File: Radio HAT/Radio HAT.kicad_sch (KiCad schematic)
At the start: 5 parts, among them J1 Raspberry_Pi_2_3, J2 Coax SMA, U1 RFM98PW

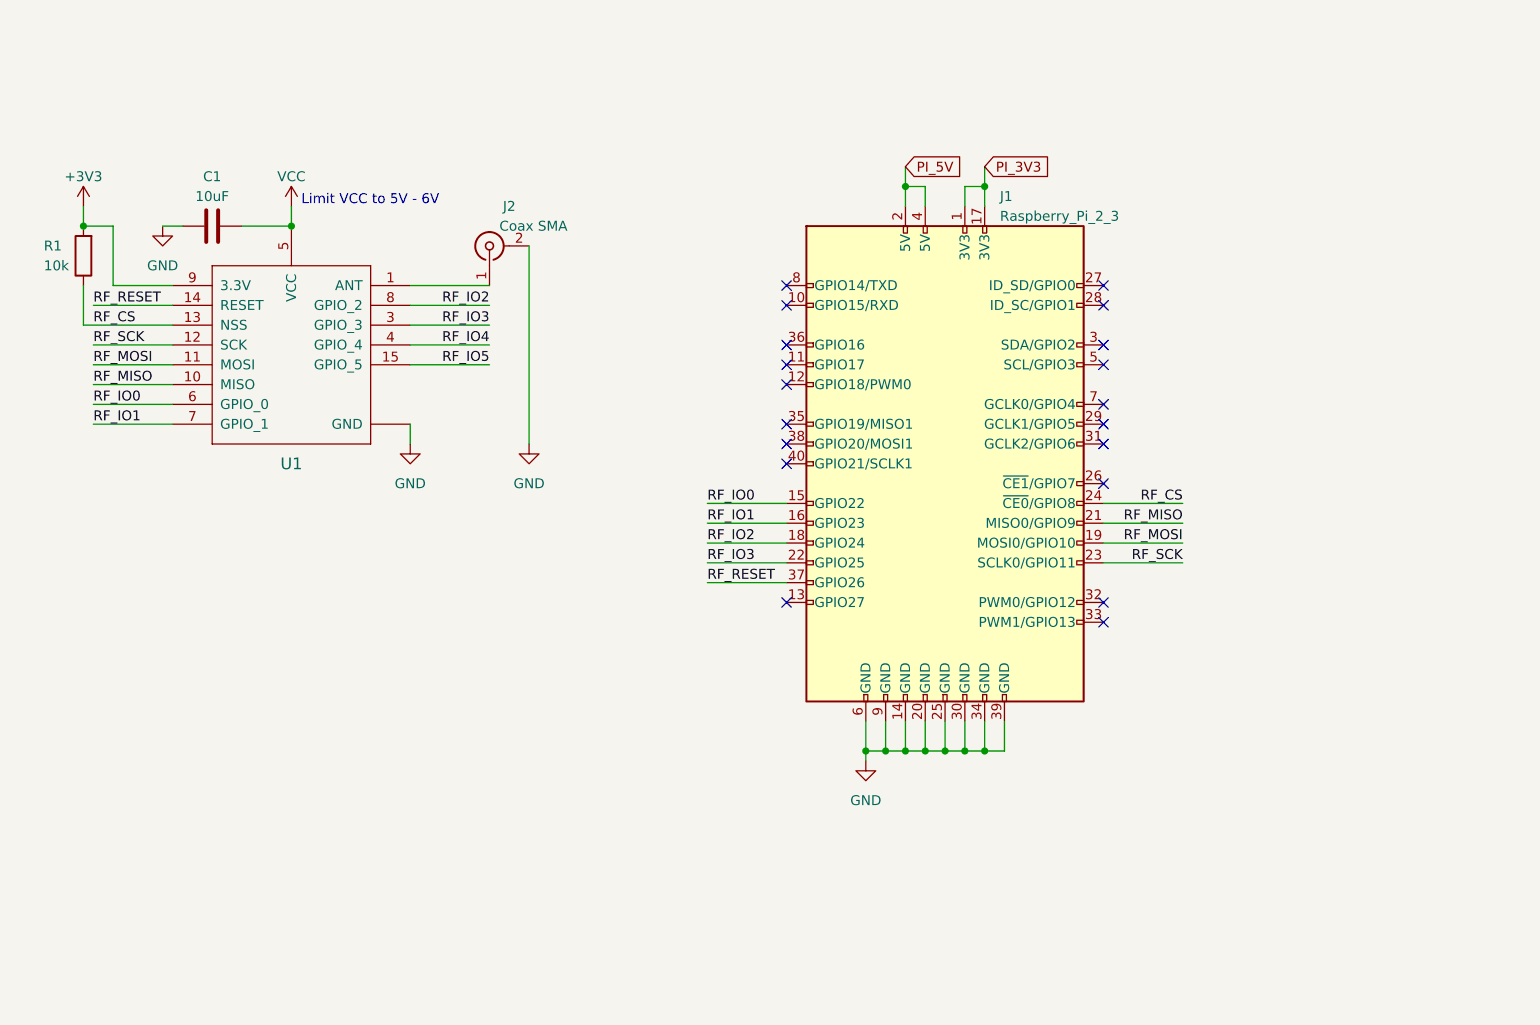
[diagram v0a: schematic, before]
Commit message: Finished schematic, started board layout
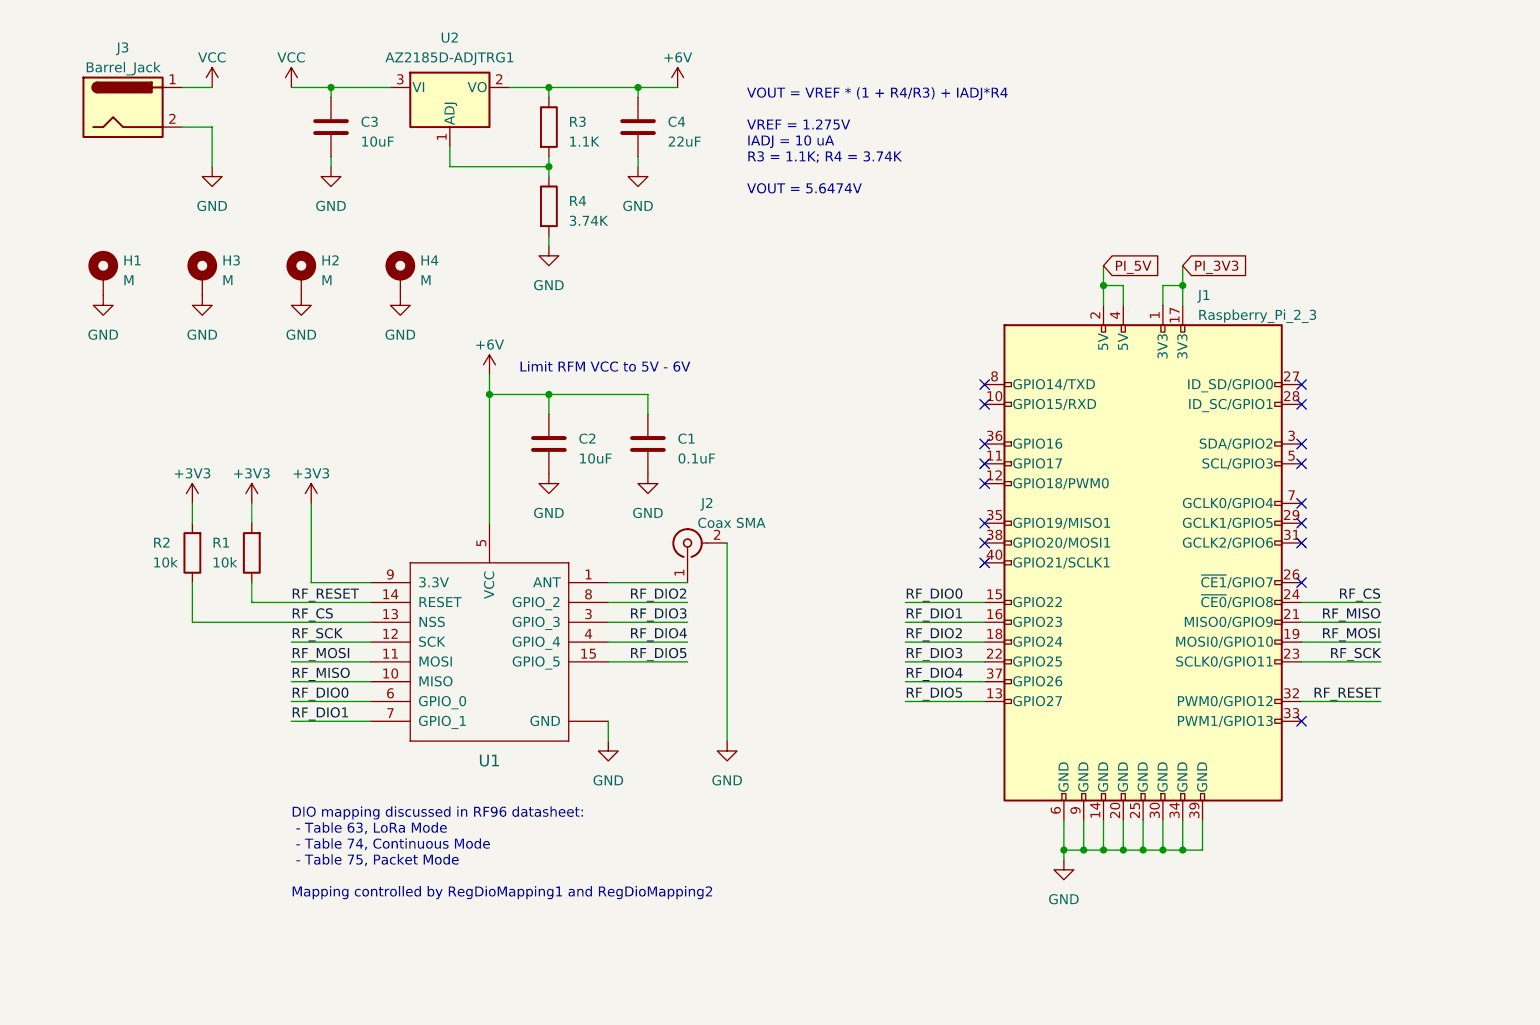
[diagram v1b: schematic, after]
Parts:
- added C2, C3: 10uF, Capacitor_SMD:C_0805_2012Metric_Pad1.18x1.45mm_HandSolder, symbol Device:C
- added C4: 22uF, Capacitor_SMD:C_0805_2012Metric_Pad1.18x1.45mm_HandSolder, symbol Device:C
- added H1, H2, H3, H4: M, MountingHole:MountingHole_2.7mm_M2.5_Pad_Via, symbol Mechanical:MountingHole_Pad
- added J3: Barrel_Jack, Connector_BarrelJack:BarrelJack_Horizontal, symbol Connector:Barrel_Jack
- added R2: 10k, Resistor_SMD:R_0805_2012Metric_Pad1.20x1.40mm_HandSolder, symbol Device:R
- added R3: 1.1K, Resistor_SMD:R_0805_2012Metric_Pad1.20x1.40mm_HandSolder, symbol Device:R
- added R4: 3.74K, Resistor_SMD:R_0805_2012Metric_Pad1.20x1.40mm_HandSolder, symbol Device:R
- added U2: AZ2185D-ADJTRG1, Package_TO_SOT_SMD:TO-252-2, symbol Regulator_Linear:NCP1117-ADJ_TO252
- C1: value 10uF -> 0.1uF; footprint (none) -> Capacitor_SMD:C_0805_2012Metric_Pad1.18x1.45mm_HandSolder
- J1: footprint (none) -> Connector_PinSocket_2.54mm:PinSocket_2x20_P2.54mm_Vertical
- J2: footprint (none) -> Connector_Coaxial:SMA_Amphenol_901-144_Vertical
- R1: footprint (none) -> Resistor_SMD:R_0805_2012Metric_Pad1.20x1.40mm_HandSolder
- U1: footprint custom-footprints:RFM95PW -> Mainboard:RFM95PW
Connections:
- net RF_IO5 is gone; now on net RF_DIO5: U1.15 (GPIO_5)
- net +3V3: now also R2.2
- net GND: now also C1.2, C2.2, C3.2, C4.2, H1.1, H2.1, H3.1, H4.1, J3.2, R4.2; no longer C1.1
- net RF_CS: now also R2.1; no longer R1.1
- net RF_RESET: now also J1.32 (PWM0/GPIO12), R1.1; no longer J1.37 (GPIO26)
- net VCC: now also C3.1, J3.1, U2.3 (VI); no longer C1.2, U1.5 (VCC)
- net RF_DIO5: now reaches J1.13 (GPIO27)
- net RF_IO0 renamed RF_DIO0
- net RF_IO1 renamed RF_DIO1
- net RF_IO2 renamed RF_DIO2
- net RF_IO3 renamed RF_DIO3
- net RF_IO4 renamed RF_DIO4
- net RF_DIO4: now also J1.37 (GPIO26)
- new net: R3.2, R4.1, U2.1 (ADJ)
- new net +6V: C1.1, C2.1, C4.1, R3.1, U1.5 (VCC), U2.2 (VO)
- no-connect marks 19 -> 17
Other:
- note added: "DIO mapping discussed in RF96 datasheet: - Table 63, LoRa Mode - Table 74, Continuous Mode - Table 75, Packet Mode Mapping controlled by RegDioMapping1 and RegDioMapping2"
- note added: "Limit RFM VCC to 5V - 6V"
- note added: "VOUT = VREF * (1 + R4/R3) + IADJ*R4 VREF = 1.275V IADJ = 10 uA R3 = 1.1K; R4 = 3.74K VOUT = 5.6474V"
- note removed: "Limit VCC to 5V - 6V"
- moved on the sheet: J1, J2, R1, U1

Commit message: Finished board design
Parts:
- removed H3, H4: M, MountingHole:MountingHole_2.7mm_M2.5_Pad_Via, symbol Mechanical:MountingHole_Pad
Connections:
- net RF_DIO0: now also J1.35 (GPIO19/MISO1); no longer J1.15 (GPIO22)
- net RF_DIO1: now also J1.38 (GPIO20/MOSI1); no longer J1.16 (GPIO23)
- net RF_DIO2: now also J1.40 (GPIO21/SCLK1); no longer J1.18 (GPIO24)
- net RF_DIO3: now also J1.33 (PWM1/GPIO13); no longer J1.22 (GPIO25)
- net RF_DIO5: now also J1.36 (GPIO16); no longer J1.13 (GPIO27)
- net RF_ANT: now reaches J2.1 (In), U1.1 (ANT)
- net REG_ADJ: now reaches R3.2, R4.1, U2.1 (ADJ)
- net PI_3V3: no longer names the net of J1.1 (3V3)
- net PI_3V3: no longer J1.17 (3V3)
- net PI_5V: no longer names the net of J1.2 (5V)
- net PI_5V: no longer J1.4 (5V)
- no-connect marks 17 -> 21
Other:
- moved on the sheet: H1, J2

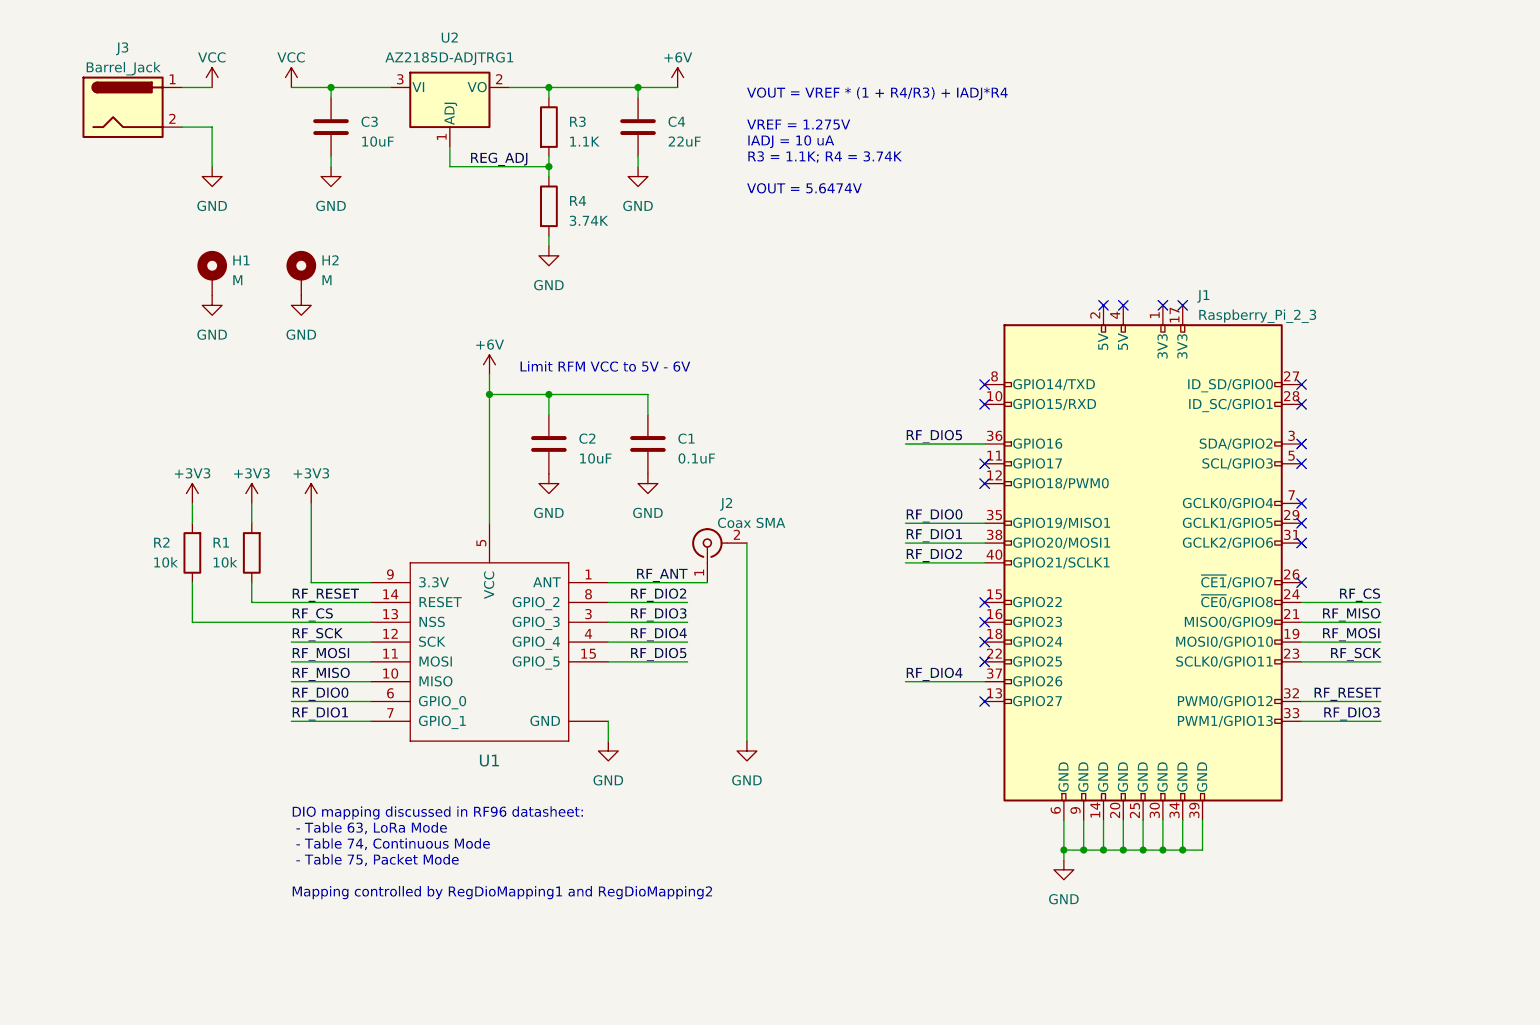
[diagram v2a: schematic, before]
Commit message: Implemented changes from PR review
Changes implemented:
 - added schematic documentation and page settings
 - fixed PCB silkscreen
 - added board rev. and information on back silkscreen
 - added 3D models, generated 3D model for board
 - generated HTML BOM
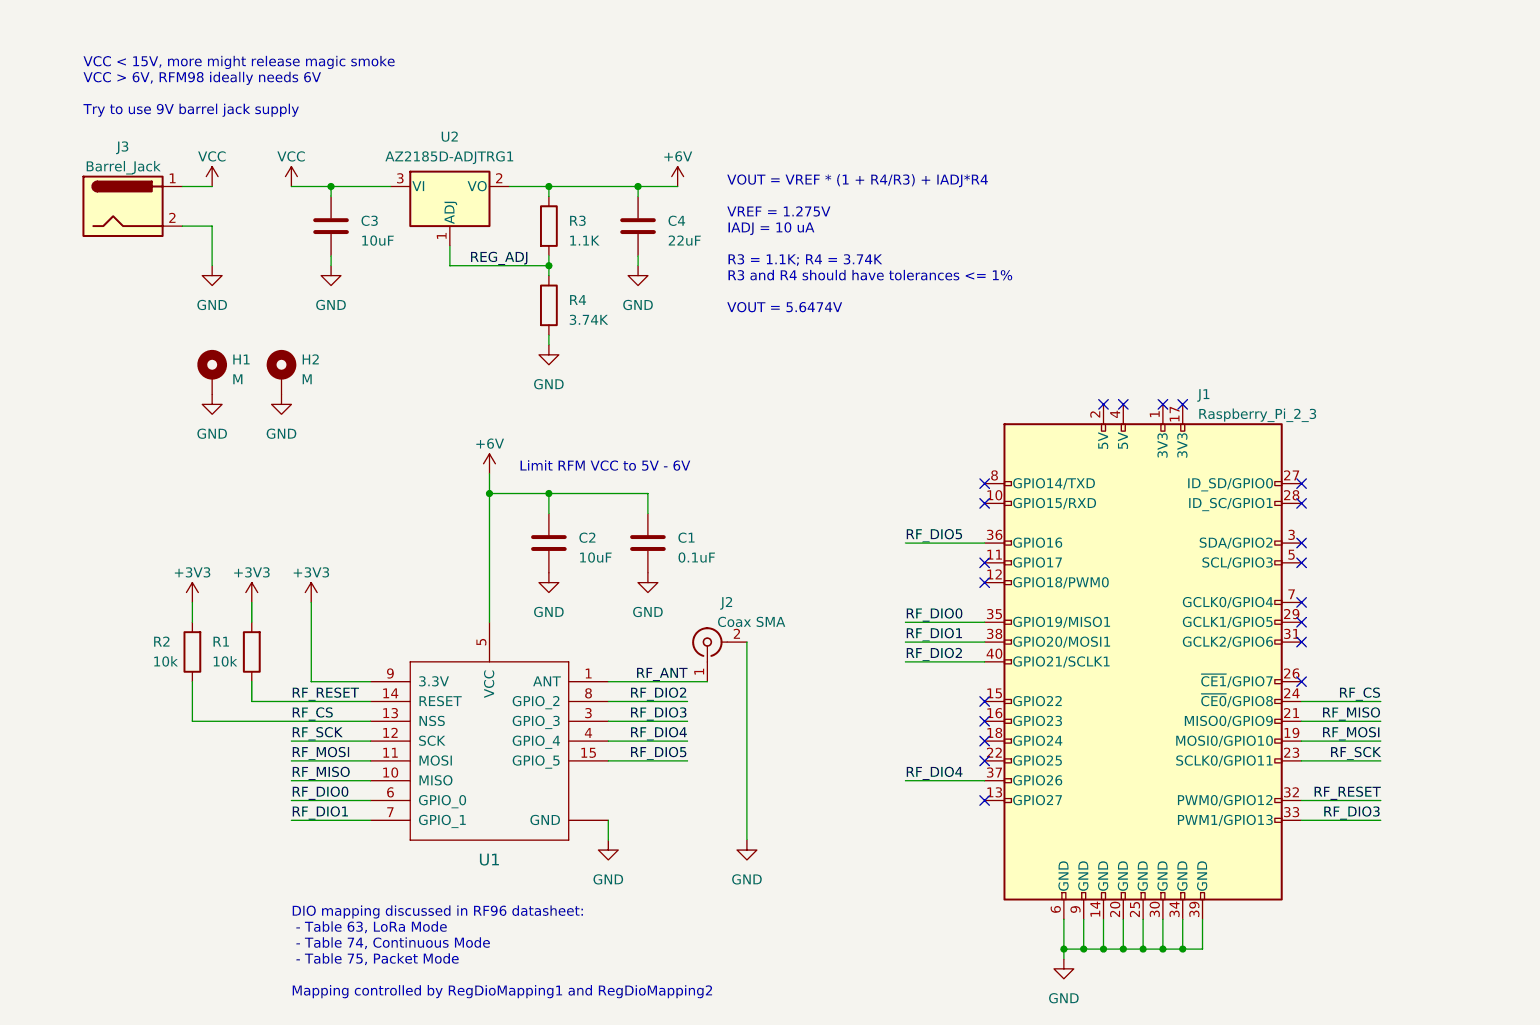
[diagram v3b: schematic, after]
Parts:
- removed U1: RFM98PW, Mainboard:RFM95PW, symbol Mainboard:RFM98PW
- removed U2: AZ2185D-ADJTRG1, Package_TO_SOT_SMD:TO-252-2, symbol Regulator_Linear:NCP1117-ADJ_TO252
- added U1: RFM98PW, RF_Module_HOPERF:RFM95PW, symbol RF_Module_HOPERF:RFM98PW
- added U2: AZ2185D-ADJTRG1, Package_TO_SOT_SMD:TO-252-2, symbol Regulator_Linear:LM317_TO-252
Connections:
- net +3V3: now also U1.9 (3.3V)
- net +6V: now also U1.5 (VCC), U2.2 (VO)
- net GND: now also U1.16 (GND), U1.17 (GND), U1.2 (GND)
- net REG_ADJ: now also U2.1 (ADJ)
- net RF_ANT: now also U1.1 (ANT)
- net RF_CS: now also U1.13 (NSS)
- net RF_DIO0: now also U1.6 (GPIO_0)
- net RF_DIO1: now also U1.7 (GPIO_1)
- net RF_DIO2: now also U1.8 (GPIO_2)
- net RF_DIO3: now also U1.3 (GPIO_3)
- net RF_DIO4: now also U1.4 (GPIO_4)
- net RF_DIO5: now also U1.15 (GPIO_5)
- net RF_MISO: now also U1.10 (MISO)
- net RF_MOSI: now also U1.11 (MOSI)
- net RF_RESET: now also U1.14 (RESET)
- net RF_SCK: now also U1.12 (SCK)
- net VCC: now also U2.3 (VI)
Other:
- note added: "VCC < 15V, more might release magic smoke VCC > 6V, RFM98 ideally needs 6V Try to use 9V barrel jack supply"
- note added: "VOUT = VREF * (1 + R4/R3) + IADJ*R4 VREF = 1.275V IADJ = 10 uA R3 = 1.1K; R4 = 3.74K R3 and R4 should have tolerances <= 1% VOUT = 5.6474V"
- note removed: "VOUT = VREF * (1 + R4/R3) + IADJ*R4 VREF = 1.275V IADJ = 10 uA R3 = 1.1K; R4 = 3.74K VOUT = 5.6474V"
- company: (none) -> Carnegie Mellon University
- title: (none) -> Argus-1 Ground Station
- moved on the sheet: C1, C2, C3, C4, H1, H2, J1, J2, J3, R1, R2, R3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
